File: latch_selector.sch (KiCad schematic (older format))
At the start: 25 parts, among them SW1 Line Selection, SW3 Step, SW4 Run/Step Mode, U1 74HCT138, U10 LMC555xM, U11 74HCT00, U12 74HCT74, U2 74HCT151, U6 74HCT32

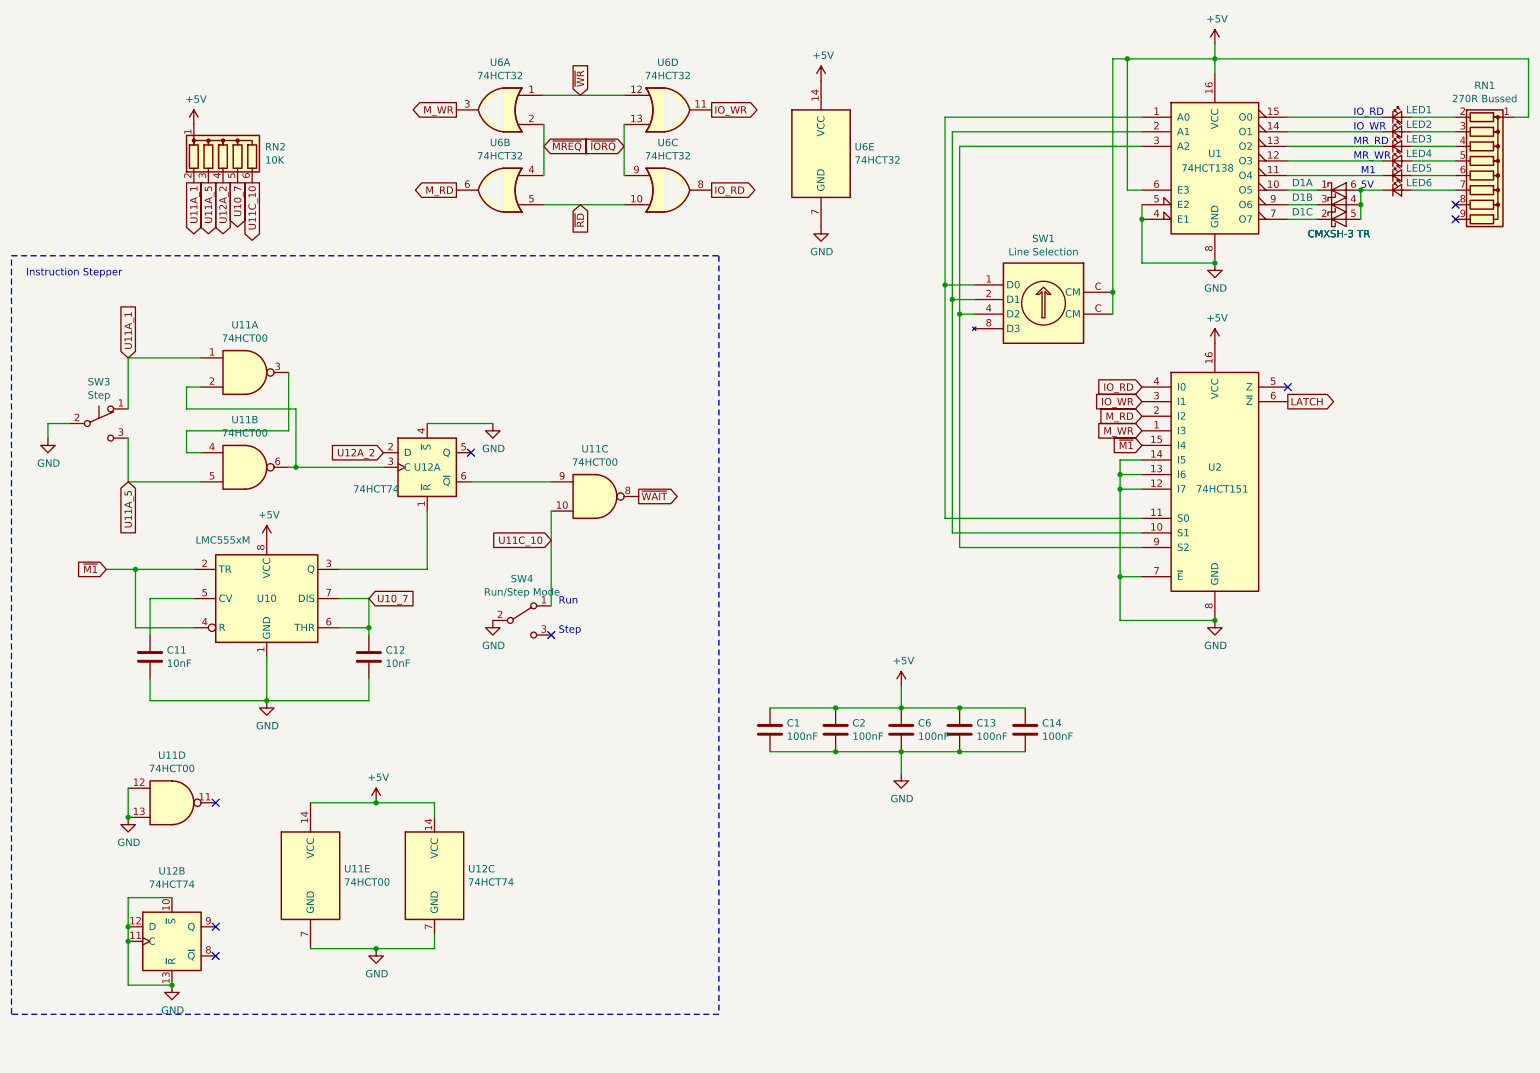
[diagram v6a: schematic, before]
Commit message: trace cleanup
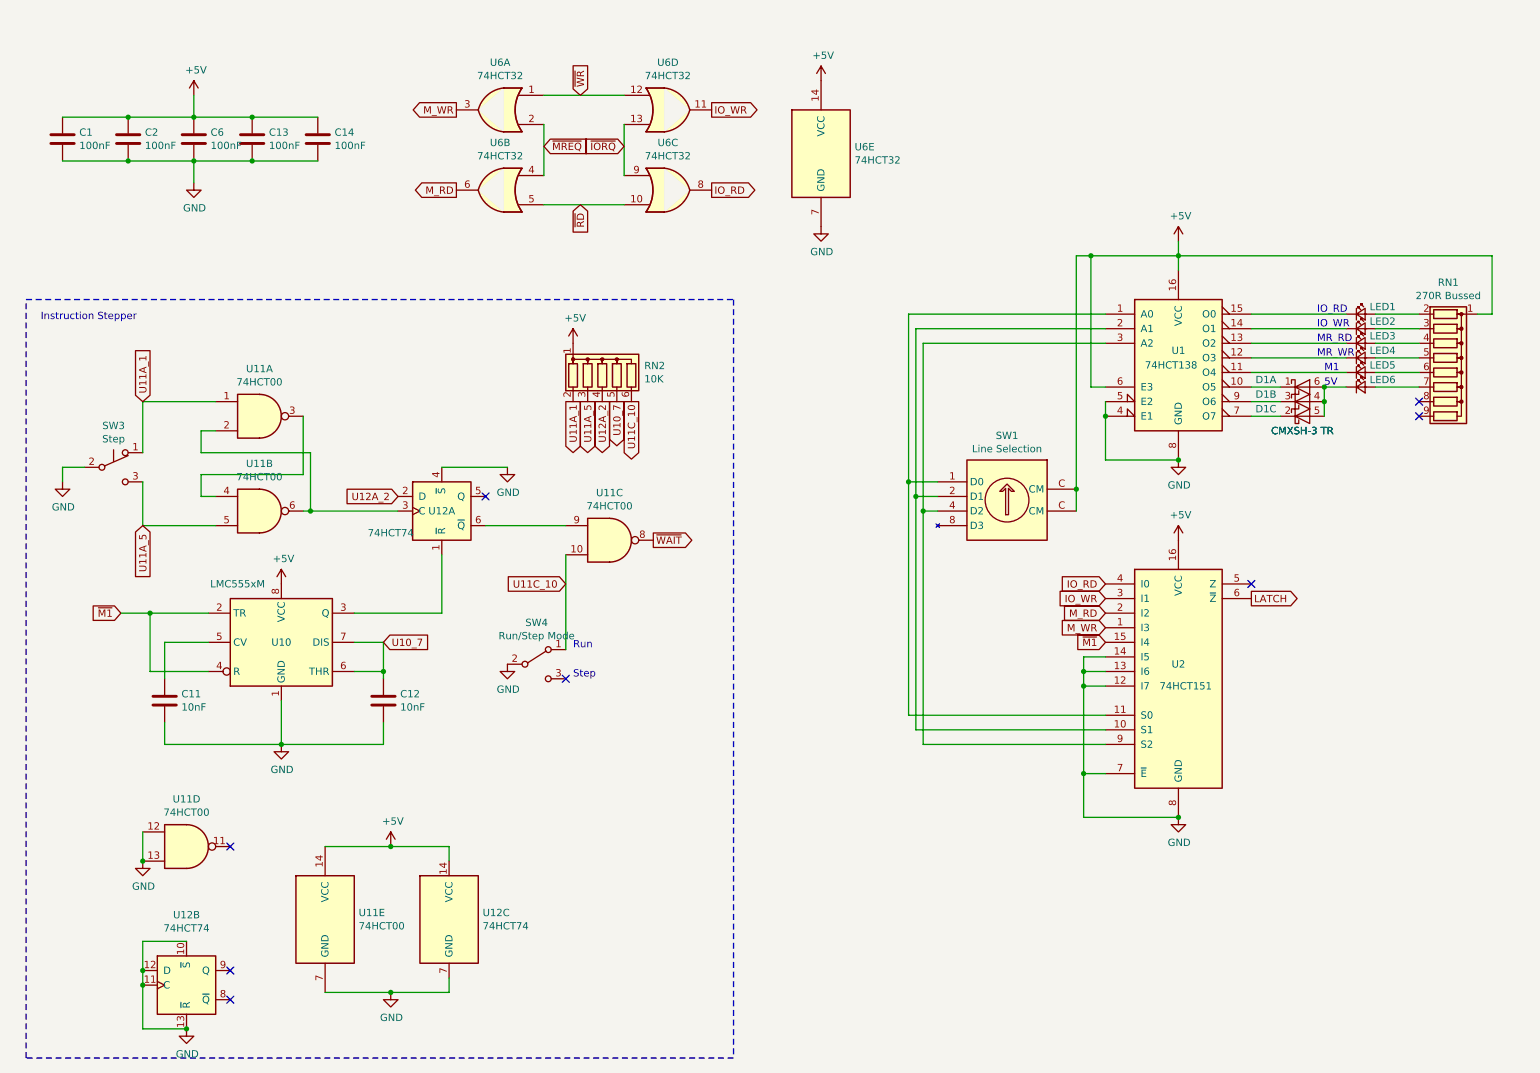
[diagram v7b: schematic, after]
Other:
- moved on the sheet: C1, C11, C12, C13, C14, C2, C6, D1A, D1B, D1C, LED1, LED2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

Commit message: use reset to clear the displays
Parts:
- removed unit 4 of U11
- LED1, LED2, LED3, LED4, LED5, LED6: SPURL - -> https://www.mouser.com/ProductDetail/ROHM-Semiconductor/SML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
- RN2: footprint Resistor_THT:R_Array_SIP6 -> Resistor_THT:R_Array_SIP7; symbol Device:R_Network05 -> Device:R_Network06
- SW1: SPURL - -> https://www.mouser.com/ProductDetail/Grayhill/94HBB08RAT?qs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
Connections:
- net U10_7 renamed RN2_4
- net U11A_1 renamed RN2_1
- net U11A_5 renamed RN2_6
- net RN2_6: now also RN2.7 (R6); no longer RN2.3 (R2)
- net U11C_10 renamed RN2_5
- net U12A_2 renamed RN2_3
- new net RN2_2: RN2.3 (R2)
- no-connect marks 8 -> 7
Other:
- moved on the sheet: D1A, D1B, D1C, LED1, LED2, LED3, LED4, LED5, LED6, RN1, SW1, U1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
